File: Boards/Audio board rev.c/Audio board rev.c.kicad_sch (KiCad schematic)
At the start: 109 parts, among them J1 CEC card edge connector large, U1 6821, U10 LM324, U11 MC1458, U2 LM339, U3 LM339, U4 ULN2003A, U5 DAC-08, U6 DAC-08, U9 LM324

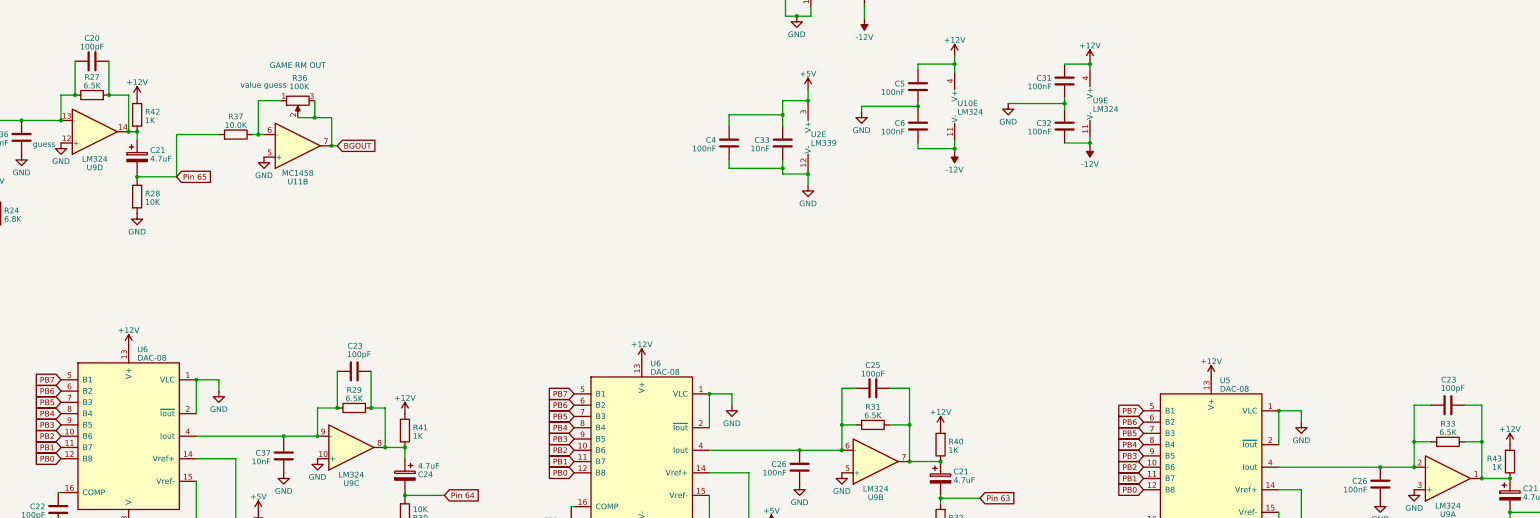
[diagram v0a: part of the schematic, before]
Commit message: tweaked copper fills on revc
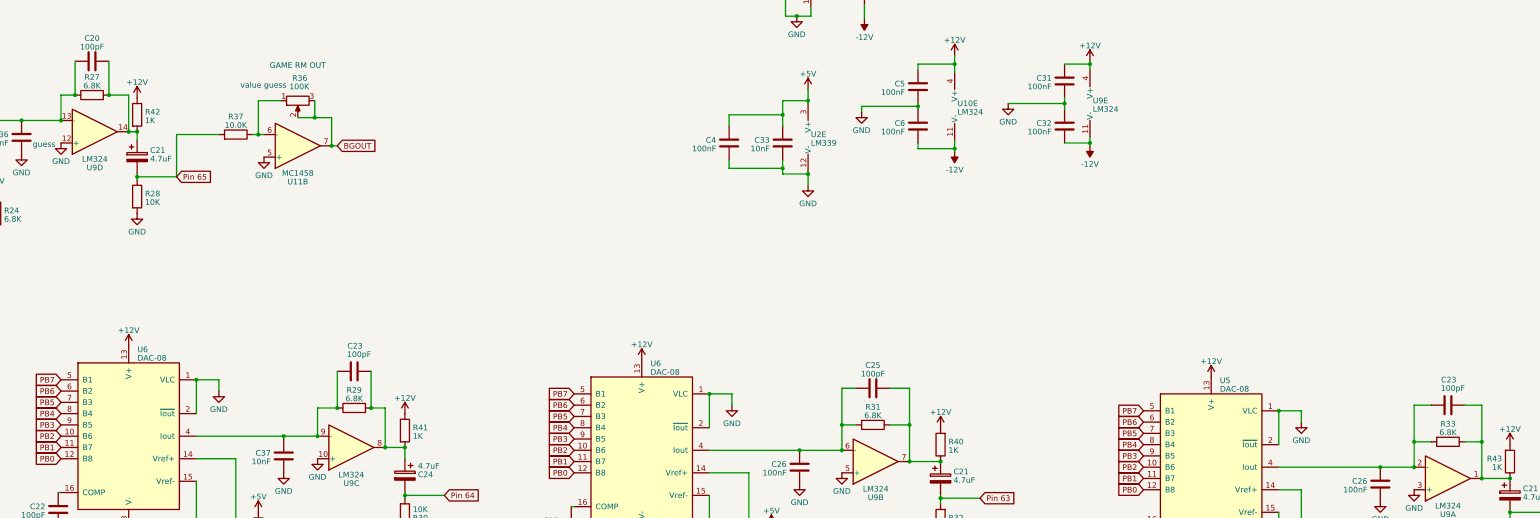
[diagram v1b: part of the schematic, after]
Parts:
- R27, R29, R31, R33: value 6.5K -> 6.8K
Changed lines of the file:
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@@
       (effects (font (size 1.27 1.27)))
     )
-    (property "Value" "6.5K" (at 316.23 289.9951 90)
+    (property "Value" "6.8K" (at 316.23 289.9951 90)
       (effects (font (size 1.27 1.27)))
     )
@@
       (effects (font (size 1.27 1.27)))
     )
-    (property "Value" "6.5K" (at 445.77 293.8051 90)
+    (property "Value" "6.8K" (at 445.77 293.8051 90)
       (effects (font (size 1.27 1.27)))
     )
@@
       (effects (font (size 1.27 1.27)))
     )
-    (property "Value" "6.5K" (at 199.39 286.1851 90)
+    (property "Value" "6.8K" (at 199.39 286.1851 90)
       (effects (font (size 1.27 1.27)))
     )
@@
       (effects (font (size 1.27 1.27)))
     )
-    (property "Value" "6.5K" (at 140.335 215.7001 90)
-      (effects (font (size 1.27 1.27)))
-    )
+    (property "Value" "6.8K" (at 140.335 215.7001 90)
+      (effects (font (size 1.27 1.27)))
+    )

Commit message: labeled pins 64 and 65
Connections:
- net Pin 64 renamed R2R_audio_AGC
- net Pin 65 renamed BGOUT_AGC
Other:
- moved on the sheet: C22, C23, C24, C37, R24, R29, R30, R41, U6, U9C

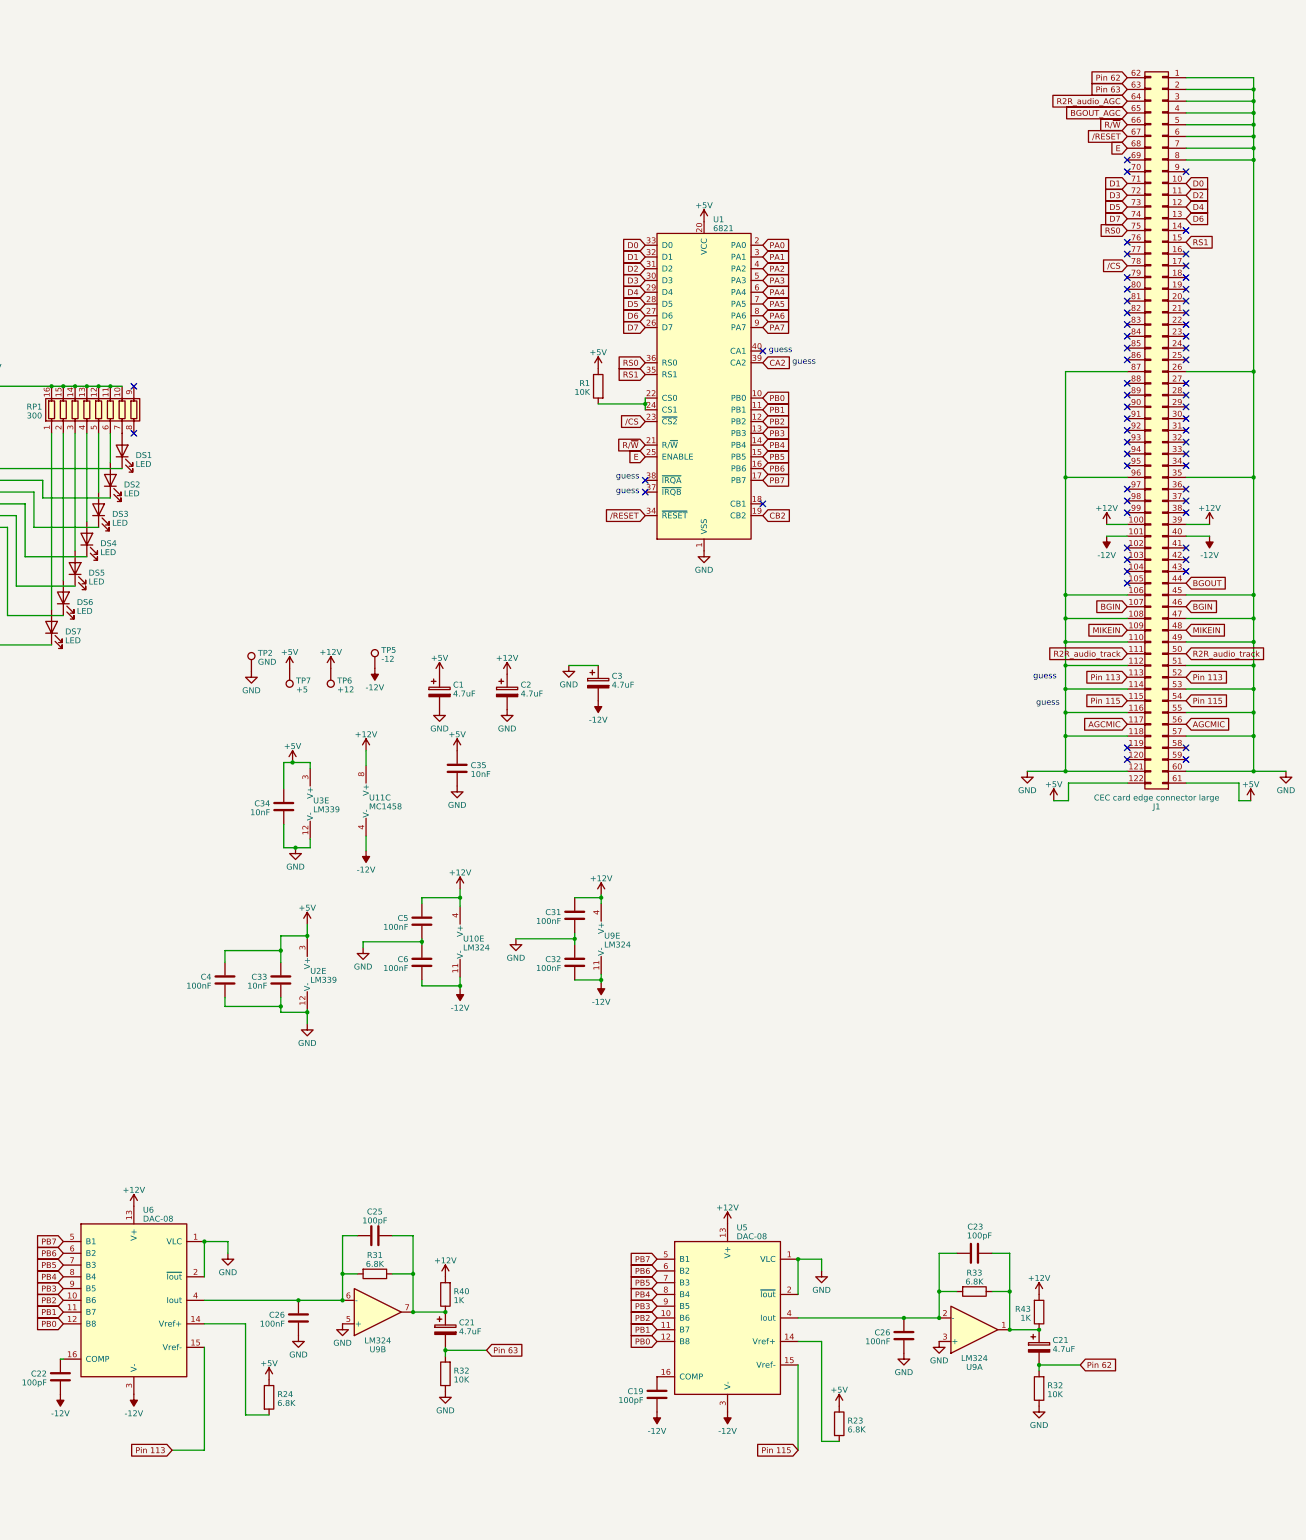
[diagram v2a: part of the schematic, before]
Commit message: revised all net names to reflect new information about 4 channel audio system
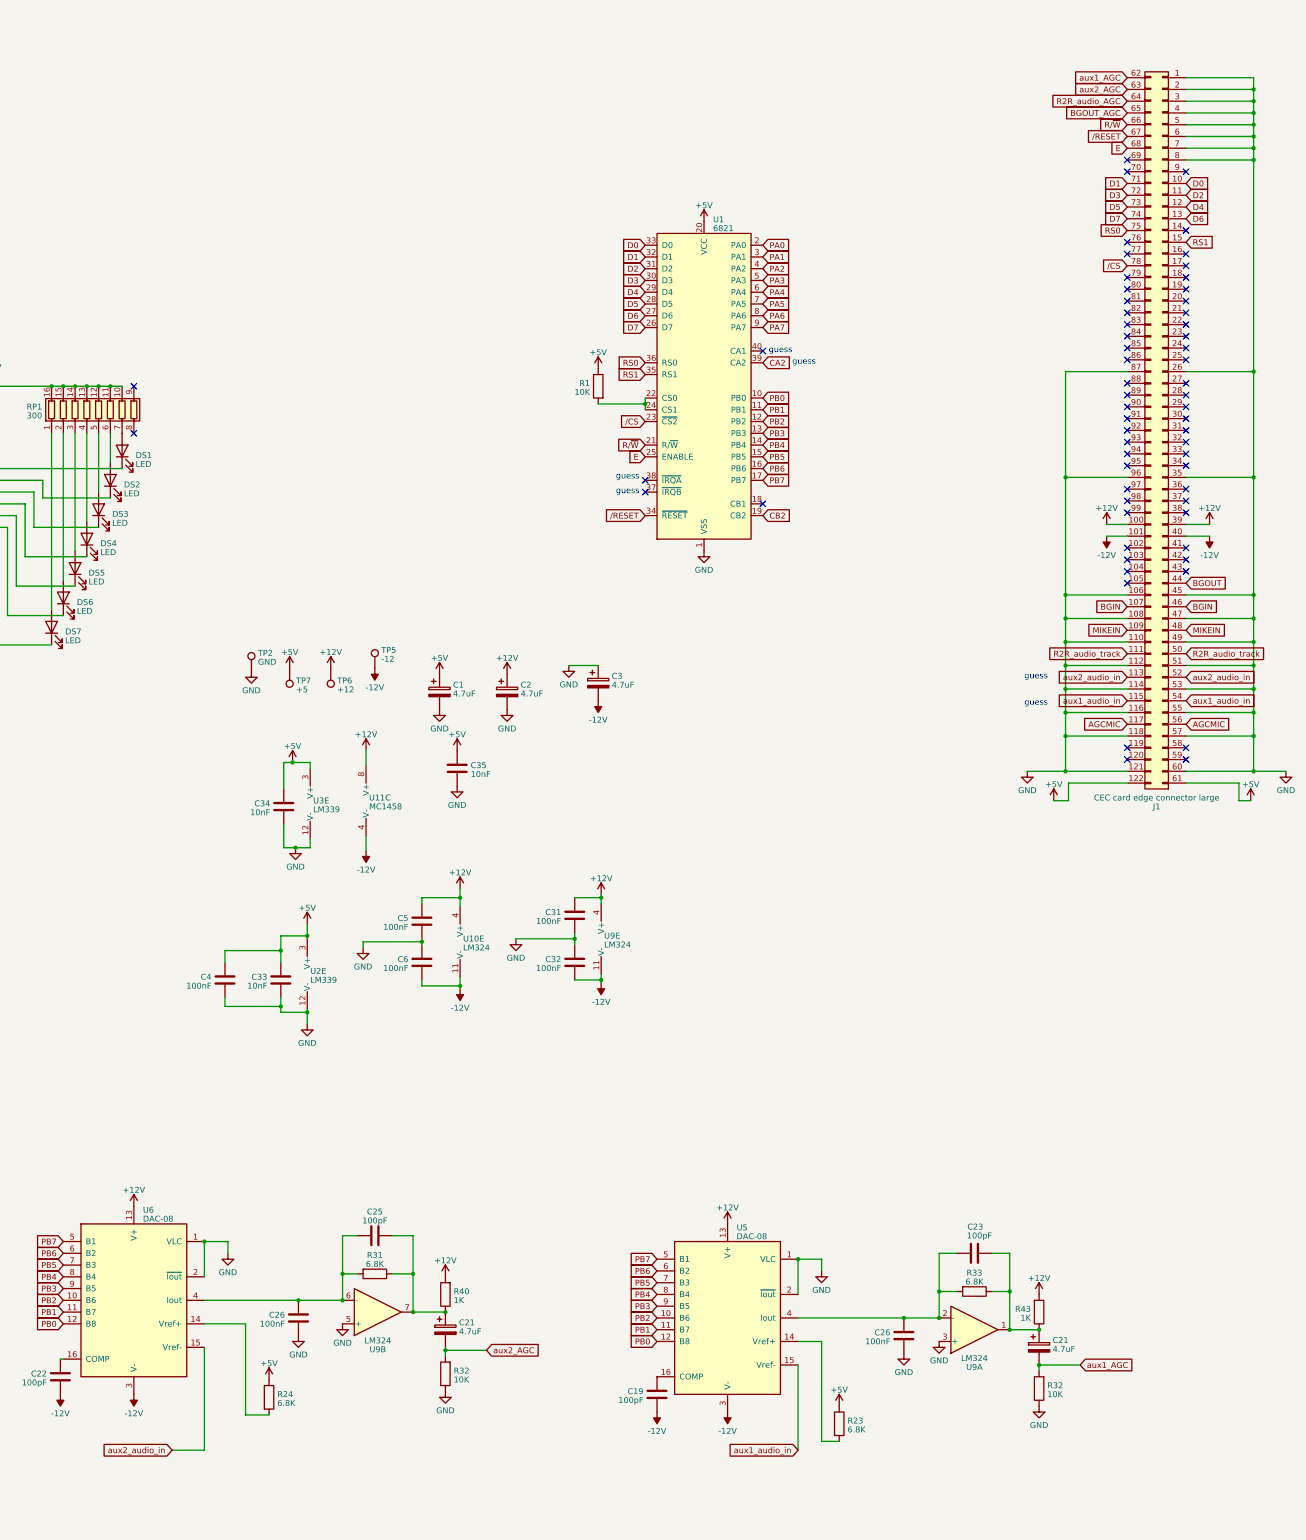
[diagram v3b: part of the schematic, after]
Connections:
- net Pin 113 renamed aux2_audio_in
- net Pin 115 renamed aux1_audio_in
- net Pin 62 renamed aux1_AGC
- net Pin 63 renamed aux2_AGC
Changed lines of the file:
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@@
     (stroke (width 0) (type default))
   )
-  (text "guess" (at 464.185 169.545 0)
+  (text "guess" (at 461.645 169.545 0)
     (effects (font (size 1.27 1.27)) (justify right bottom))
   )
@@
     (effects (font (size 1.27 1.27)) (justify left bottom))
   )
-  (text "guess" (at 463.55 163.83 0)
+  (text "guess" (at 461.645 163.83 0)
     (effects (font (size 1.27 1.27)) (justify right bottom))
   )
@@
     )
   )
-  (global_label "Pin 115" (shape input) (at 478.79 168.275 180) (fields_autoplaced)
-    (effects (font (size 1.27 1.27)) (justify right))
-    (property "Intersheetrefs" "${INTERSHEET_REFS}" (at 468.2643 168.275 0)
+  (global_label "aux1_audio_in" (shape input) (at 478.79 168.275 180) (fields_autoplaced)
+    (effects (font (size 1.27 1.27)) (justify right))
+    (property "Intersheetrefs" "${INTERSHEET_REFS}" (at 462.4588 168.275 0)
       (effects (font (size 1.27 1.27)) (justify right) hide)
     )
@@
     )
   )
-  (global_label "Pin 113" (shape input) (at 272.415 330.2 180) (fields_autoplaced)
-    (effects (font (size 1.27 1.27)) (justify right))
-    (property "Intersheetrefs" "${INTERSHEET_REFS}" (at 261.8893 330.2 0)
+  (global_label "aux2_audio_in" (shape input) (at 272.415 330.2 180) (fields_autoplaced)
+    (effects (font (size 1.27 1.27)) (justify right))
+    (property "Intersheetrefs" "${INTERSHEET_REFS}" (at 256.0838 330.2 0)
       (effects (font (size 1.27 1.27)) (justify right) hide)
     )
@@
     )
   )
-  (global_label "Pin 63" (shape input) (at 340.36 308.61 0) (fields_autoplaced)
-    (effects (font (size 1.27 1.27)) (justify left))
-    (property "Intersheetrefs" "${INTERSHEET_REFS}" (at 349.6762 308.61 0)
+  (global_label "aux2_AGC" (shape input) (at 340.36 308.61 0) (fields_autoplaced)
+    (effects (font (size 1.27 1.27)) (justify left))
+    (property "Intersheetrefs" "${INTERSHEET_REFS}" (at 352.3976 308.61 0)
       (effects (font (size 1.27 1.27)) (justify left) hide)
     )
@@
     )
   )
-  (global_label "Pin 115" (shape input) (at 491.49 168.275 0) (fields_autoplaced)
-    (effects (font (size 1.27 1.27)) (justify left))
-    (property "Intersheetrefs" "${INTERSHEET_REFS}" (at 502.0157 168.275 0)
+  (global_label "aux1_audio_in" (shape input) (at 491.49 168.275 0) (fields_autoplaced)
+    (effects (font (size 1.27 1.27)) (justify left))
+    (property "Intersheetrefs" "${INTERSHEET_REFS}" (at 507.8212 168.275 0)
       (effects (font (size 1.27 1.27)) (justify left) hide)
     )
@@
     )
   )
-  (global_label "Pin 63" (shape input) (at 478.79 36.195 180) (fields_autoplaced)
-    (effects (font (size 1.27 1.27)) (justify right))
-    (property "Intersheetrefs" "${INTERSHEET_REFS}" (at 469.4738 36.195 0)
+  (global_label "aux2_AGC" (shape input) (at 478.79 36.195 180) (fields_autoplaced)
+    (effects (font (size 1.27 1.27)) (justify right))
+    (property "Intersheetrefs" "${INTERSHEET_REFS}" (at 466.7524 36.195 0)
       (effects (font (size 1.27 1.27)) (justify right) hide)
     )
@@
     )
   )
-  (global_label "Pin 113" (shape input) (at 478.79 163.195 180) (fields_autoplaced)
-    (effects (font (size 1.27 1.27)) (justify right))
-    (property "Intersheetrefs" "${INTERSHEET_REFS}" (at 468.2643 163.195 0)
+  (global_label "aux2_audio_in" (shape input) (at 478.79 163.195 180) (fields_autoplaced)
+    (effects (font (size 1.27 1.27)) (justify right))
+    (property "Intersheetrefs" "${INTERSHEET_REFS}" (at 462.4588 163.195 0)
       (effects (font (size 1.27 1.27)) (justify right) hide)
     )
@@
     )
   )
-  (global_label "Pin 115" (shape input) (at 407.67 330.2 180) (fields_autoplaced)
-    (effects (font (size 1.27 1.27)) (justify right))
-    (property "Intersheetrefs" "${INTERSHEET_REFS}" (at 397.1443 330.2 0)
+  (global_label "aux1_audio_in" (shape input) (at 407.67 330.2 180) (fields_autoplaced)
+    (effects (font (size 1.27 1.27)) (justify right))
+    (property "Intersheetrefs" "${INTERSHEET_REFS}" (at 391.3388 330.2 0)
       (effects (font (size 1.27 1.27)) (justify right) hide)
     )
@@
     )
   )
-  (global_label "Pin 62" (shape input) (at 468.63 311.785 0) (fields_autoplaced)
-    (effects (font (size 1.27 1.27)) (justify left))
-    (property "Intersheetrefs" "${INTERSHEET_REFS}" (at 477.9462 311.785 0)
+  (global_label "aux1_AGC" (shape input) (at 468.63 311.785 0) (fields_autoplaced)
+    (effects (font (size 1.27 1.27)) (justify left))
+    (property "Intersheetrefs" "${INTERSHEET_REFS}" (at 480.6676 311.785 0)
       (effects (font (size 1.27 1.27)) (justify left) hide)
     )
@@
     )
   )
-  (global_label "Pin 62" (shape input) (at 478.79 33.655 180) (fields_autoplaced)
-    (effects (font (size 1.27 1.27)) (justify right))
-    (property "Intersheetrefs" "${INTERSHEET_REFS}" (at 469.4738 33.655 0)
+  (global_label "aux1_AGC" (shape input) (at 478.79 33.655 180) (fields_autoplaced)
+    (effects (font (size 1.27 1.27)) (justify right))
+    (property "Intersheetrefs" "${INTERSHEET_REFS}" (at 466.7524 33.655 0)
       (effects (font (size 1.27 1.27)) (justify right) hide)
     )
@@
     )
   )
-  (global_label "Pin 113" (shape input) (at 491.49 163.195 0) (fields_autoplaced)
-    (effects (font (size 1.27 1.27)) (justify left))
-    (property "Intersheetrefs" "${INTERSHEET_REFS}" (at 502.0157 163.195 0)
-      (effects (font (size 1.27 1.27)) (justify left) hide)
-    )
+  (global_label "aux2_audio_in" (shape input) (at 491.49 163.195 0) (fields_autoplaced)
+    (effects (font (size 1.27 1.27)) (justify left))
+    (property "Intersheetrefs" "${INTERSHEET_REFS}" (at 507.8212 163.195 0)
+      (effects (font (size 1.27 1.27)) (justify left) hide)
+    )
